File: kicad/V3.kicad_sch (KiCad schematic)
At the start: 5 parts

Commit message: switch
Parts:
- added SW1: Slide_Switch_SPDT_P3mm_10x5x10mm, PCM_SL_Devices:Slide_Switch_SPDT_P3mm_10x5x10mm, symbol PCM_SL_Devices:Slide_Switch_SPDT_P3mm_10x5x10mm
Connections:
- net -3V3: now also SW1.1; no longer U1.1 (Out+)
- new net: SW1.2, U1.1 (Out+)
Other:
- moved on the sheet: BT1
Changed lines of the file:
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@@
 	)
 	(junction
-		(at 218.44 64.77)
+		(at 259.08 39.37)
 		(diameter 0)
 		(color 0 0 0 0)
@@
 	(wire
 		(pts
-			(xy 231.14 53.34) (xy 234.95 53.34)
+			(xy 271.78 27.94) (xy 275.59 27.94)
 		)
 		(stroke
@@
 	(wire
 		(pts
+			(xy 247.65 29.21) (xy 248.92 29.21)
+		)
+		(stroke
+			(width 0)
+			(type default)
+		)
+	)
+	(wire
+		(pts
 			(xy 80.01 50.8) (xy 80.01 72.39)
 		)
@@
 	(wire
 		(pts
-			(xy 218.44 66.04) (xy 218.44 64.77)
+			(xy 259.08 40.64) (xy 259.08 39.37)
 		)
 		(stroke
@@
 	(wire
 		(pts
-			(xy 231.14 53.34) (xy 231.14 54.61)
+			(xy 271.78 27.94) (xy 271.78 29.21)
 		)
 		(stroke
@@
 	(wire
 		(pts
-			(xy 208.28 64.77) (xy 218.44 64.77)
+			(xy 248.92 39.37) (xy 259.08 39.37)
 		)
 		(stroke
@@
 	(wire
 		(pts
-			(xy 208.28 59.69) (xy 208.28 64.77)
+			(xy 248.92 34.29) (xy 248.92 39.37)
 		)
 		(stroke
@@
 	(wire
 		(pts
-			(xy 231.14 60.96) (xy 231.14 59.69)
+			(xy 271.78 35.56) (xy 271.78 34.29)
 		)
 		(stroke
@@
 	(wire
 		(pts
-			(xy 228.6 54.61) (xy 231.14 54.61)
+			(xy 269.24 29.21) (xy 271.78 29.21)
 		)
 		(stroke
@@
 	(wire
 		(pts
-			(xy 231.14 60.96) (xy 234.95 60.96)
+			(xy 271.78 35.56) (xy 275.59 35.56)
 		)
 		(stroke
@@
 	(wire
 		(pts
-			(xy 228.6 59.69) (xy 231.14 59.69)
+			(xy 269.24 34.29) (xy 271.78 34.29)
+		)
+		(stroke
+			(width 0)
+			(type default)
+		)
+	)
+	(wire
+		(pts
+			(xy 236.22 31.75) (xy 236.22 24.13)
 		)
 		(stroke
@@
 	(symbol
 		(lib_id "Library:TP4056_usb_module")
-		(at 215.9 55.88 0)
+		(at 256.54 30.48 0)
 		(unit 1)
 		(exclude_from_sim no)
@@
 		(fields_autoplaced yes)
 		(property "Reference" "U1"
-			(at 214.63 57.15 90)
+			(at 255.27 31.75 90)
 			(effects
 				(font
@@
 		)
 		(property "Value" "~"
-			(at 220.5833 50.8 0)
+			(at 261.2233 25.4 0)
 			(effects
 				(font
@@
 		)
 		(property "Footprint" "Library:HAYATEC TP4056 LIPO CHARGING MODULE"
-			(at 215.9 55.88 0)
+			(at 256.54 30.48 0)
 			(effects
 				(font
@@
 		)
 		(property "Datasheet" ""
-			(at 215.9 55.88 0)
+			(at 256.54 30.48 0)
 			(effects
 				(font
@@
 		)
 		(property "Description" ""
-			(at 215.9 55.88 0)
+			(at 256.54 30.48 0)
 			(effects
 				(font
@@
 	(symbol
 		(lib_id "power:Earth")
-		(at 218.44 66.04 0)
+		(at 259.08 40.64 0)
 		(unit 1)
 		(exclude_from_sim no)
@@
 		(fields_autoplaced yes)
 		(property "Reference" "#PWR01"
-			(at 218.44 72.39 0)
+			(at 259.08 46.99 0)
 			(effects
 				(font
@@
 		)
 		(property "Value" "Earth"
-			(at 218.44 71.12 0)
+			(at 259.08 45.72 0)
 			(effects
 				(font
@@
 		)
 		(property "Footprint" ""
-			(at 218.44 66.04 0)
+			(at 259.08 40.64 0)
 			(effects
 				(font
@@
 		)
 		(property "Datasheet" "~"
-			(at 218.44 66.04 0)
+			(at 259.08 40.64 0)
 			(effects
 				(font
@@
 		)
 		(property "Description" "Power symbol creates a global label with name \"Earth\""
-			(at 218.44 66.04 0)
+			(at 259.08 40.64 0)
 			(effects
 				(font
@@
 	)
 	(symbol
+		(lib_id "PCM_SL_Devices:Slide_Switch_SPDT_P3mm_10x5x10mm")
+		(at 242.57 31.75 0)
+		(unit 1)
+		(exclude_from_sim no)
+		(in_bom yes)
+		(on_board yes)
+		(dnp no)
+		(fields_autoplaced yes)
+		(property "Reference" "SW1"
+			(at 241.935 24.13 0)
+			(effects
+				(font
+					(size 1.27 1.27)
+				)
+			)
+		)
+		(property "Value" "Slide_Switch_SPDT_P3mm_10x5x10mm"
+			(at 241.935 26.67 0)
+			(effects
+				(font
+					(size 1.27 1.27)
+				)
+			)
+		)
+		(property "Footprint" "PCM_SL_Devices:Slide_Switch_SPDT_P3mm_10x5x10mm"
+			(at 243.84 39.37 0)
+			(effects
+				(font
+					(size 1.27 1.27)
+				)
+				(hide yes)
+			)
+		)
+		(property "Datasheet" ""
+			(at 241.3 25.4 0)
+			(effects
+				(font
+					(size 1.27 1.27)
+				)
+				(hide yes)
+			)
+		)
+		(property "Description" "SPDT Slide Switch with 10mm length, 5mm width and 10mm hight."
+			(at 242.57 31.75 0)
+			(effects
+				(font
+					(size 1.27 1.27)
+				)
+				(hide yes)
+			)
+		)
+		(pin "2"
+		)
+		(pin "3"
+		)
+		(pin "1"
+		)
+		(instances
+			(project ""
+				(path "/55ac274f-6d39-4edb-ae03-cf051723ec39"
+					(reference "SW1")
+					(unit 1)
+				)
+			)
+		)
+	)
+	(symbol
 		(lib_id "power:VCC")
-		(at 218.44 49.53 0)
+		(at 259.08 24.13 0)
 		(unit 1)
 		(exclude_from_sim no)
@@
 		(fields_autoplaced yes)
 		(property "Reference" "#PWR03"
-			(at 218.44 53.34 0)
+			(at 259.08 27.94 0)
 			(effects
 				(font
@@
 		)
 		(property "Value" "VCC"
-			(at 218.44 44.45 0)
+			(at 259.08 19.05 0)
 			(effects
 				(font
@@
 		)
 		(property "Footprint" ""
-			(at 218.44 49.53 0)
+			(at 259.08 24.13 0)
 			(effects
 				(font
@@
 		)
 		(property "Datasheet" ""
-			(at 218.44 49.53 0)
+			(at 259.08 24.13 0)
 			(effects
 				(font
@@
 		)
 		(property "Description" "Power symbol creates a global label with name \"VCC\""
-			(at 218.44 49.53 0)
+			(at 259.08 24.13 0)
 			(effects
 				(font
@@
 	(symbol
 		(lib_id "Device:Battery_Cell")
-		(at 234.95 58.42 0)
+		(at 275.59 33.02 0)
 		(unit 1)
 		(exclude_from_sim no)
@@
 		(fields_autoplaced yes)
 		(property "Reference" "BT1"
-			(at 238.76 55.3084 0)
+			(at 279.4 29.9084 0)
 			(effects
 				(font
@@
 		)
 		(property "Value" "Battery_Cell"
-			(at 238.76 57.8484 0)
+			(at 279.4 32.4484 0)
 			(effects
 				(font
@@
 		)
 		(property "Footprint" ""
-			(at 234.95 56.896 90)
+			(at 275.59 31.496 90)
 			(effects
 				(font
@@
 		)
 		(property "Datasheet" "~"
-			(at 234.95 56.896 90)
+			(at 275.59 31.496 90)
 			(effects
 				(font
@@
 		)
 		(property "Description" "Single-cell battery"
-			(at 234.95 58.42 0)
+			(at 275.59 33.02 0)
 			(effects
 				(font
@@
 	(symbol
 		(lib_id "power:-3V3")
-		(at 208.28 54.61 0)
+		(at 236.22 24.13 0)
 		(unit 1)
 		(exclude_from_sim no)
@@
 		(fields_autoplaced yes)
 		(property "Reference" "#PWR08"
-			(at 208.28 58.42 0)
+			(at 236.22 27.94 0)
 			(effects
 				(font
@@
 		)
 		(property "Value" "-3V3"
-			(at 208.28 49.53 0)
+			(at 236.22 19.05 0)
 			(effects
 				(font
@@
 		)
 		(property "Footprint" ""
-			(at 208.28 54.61 0)
+			(at 236.22 24.13 0)
 			(effects
 				(font
@@
 		)
 		(property "Datasheet" ""
-			(at 208.28 54.61 0)
+			(at 236.22 24.13 0)
 			(effects
 				(font
@@
 		)
 		(property "Description" "Power symbol creates a global label with name \"-3V3\""
-			(at 208.28 54.61 0)
-			(effects
-				(font
+			(at 236.22 24.13 0)
+			(effects
+				(font

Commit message: fixed connections and pin#
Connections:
- net Earth: now also U1.1 (Gin), U1.3 (Out-); no longer U1.2 (Gin), U1.5 (Out-)
- net VCC: now also U1.2 (Vin); no longer U1.4 (Vin)
- net at SW1.2: now also U1.6 (Out+); no longer U1.1 (Out+)
- net at BT1.1 (+): now also U1.5 (B+); no longer U1.3 (B+)
- net at BT1.2 (-): now also U1.4 (B-); no longer U1.6 (B-)
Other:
- moved on the sheet: SW1
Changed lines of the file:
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@@
+	)
+	(junction
+		(at 259.08 39.37)
+		(diameter 0)
+		(color 0 0 0 0)
 	)
 	(junction
@@
 	)
 	(junction
-		(at 259.08 39.37)
-		(diameter 0)
-		(color 0 0 0 0)
-	)
-	(junction
 		(at 118.11 90.17)
 		(diameter 0)
@@
 	(wire
 		(pts
-			(xy 247.65 29.21) (xy 248.92 29.21)
+			(xy 242.57 29.21) (xy 248.92 29.21)
 		)
 		(stroke
@@
 	(wire
 		(pts
-			(xy 236.22 31.75) (xy 236.22 24.13)
+			(xy 231.14 31.75) (xy 231.14 24.13)
 		)
 		(stroke
@@
 			)
 		)
+		(pin "3"
+		)
+		(pin "5"
+		)
+		(pin "2"
+		)
+		(pin "6"
+		)
 		(pin "1"
 		)
-		(pin "6"
-		)
-		(pin "3"
-		)
 		(pin "4"
-		)
-		(pin "2"
-		)
-		(pin "5"
 		)
 		(instances
@@
 	(symbol
 		(lib_id "PCM_SL_Devices:Slide_Switch_SPDT_P3mm_10x5x10mm")
-		(at 242.57 31.75 0)
+		(at 237.49 31.75 0)
 		(unit 1)
 		(exclude_from_sim no)
@@
 		(fields_autoplaced yes)
 		(property "Reference" "SW1"
-			(at 241.935 24.13 0)
+			(at 236.855 24.13 0)
 			(effects
 				(font
@@
 		)
 		(property "Value" "Slide_Switch_SPDT_P3mm_10x5x10mm"
-			(at 241.935 26.67 0)
+			(at 236.855 26.67 0)
 			(effects
 				(font
@@
 		)
 		(property "Footprint" "PCM_SL_Devices:Slide_Switch_SPDT_P3mm_10x5x10mm"
-			(at 243.84 39.37 0)
+			(at 238.76 39.37 0)
 			(effects
 				(font
@@
 		)
 		(property "Datasheet" ""
-			(at 241.3 25.4 0)
+			(at 236.22 25.4 0)
 			(effects
 				(font
@@
 		)
 		(property "Description" "SPDT Slide Switch with 10mm length, 5mm width and 10mm hight."
-			(at 242.57 31.75 0)
+			(at 237.49 31.75 0)
 			(effects
 				(font
@@
 	(symbol
 		(lib_id "power:-3V3")
-		(at 236.22 24.13 0)
+		(at 231.14 24.13 0)
 		(unit 1)
 		(exclude_from_sim no)
@@
 		(fields_autoplaced yes)
 		(property "Reference" "#PWR08"
-			(at 236.22 27.94 0)
+			(at 231.14 27.94 0)
 			(effects
 				(font
@@
 		)
 		(property "Value" "-3V3"
-			(at 236.22 19.05 0)
+			(at 231.14 19.05 0)
 			(effects
 				(font
@@
 		)
 		(property "Footprint" ""
-			(at 236.22 24.13 0)
+			(at 231.14 24.13 0)
 			(effects
 				(font
@@
 		)
 		(property "Datasheet" ""
-			(at 236.22 24.13 0)
+			(at 231.14 24.13 0)
 			(effects
 				(font
@@
 		)
 		(property "Description" "Power symbol creates a global label with name \"-3V3\""
-			(at 236.22 24.13 0)
-			(effects
-				(font
+			(at 231.14 24.13 0)
+			(effects
+				(font

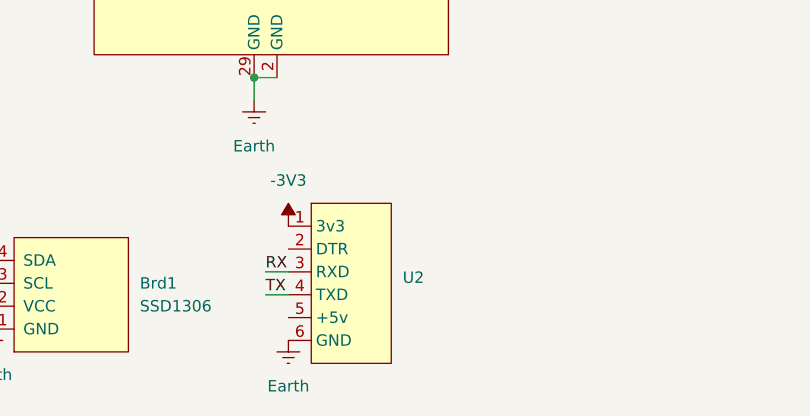
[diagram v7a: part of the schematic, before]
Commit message: changed uart-hid pinout
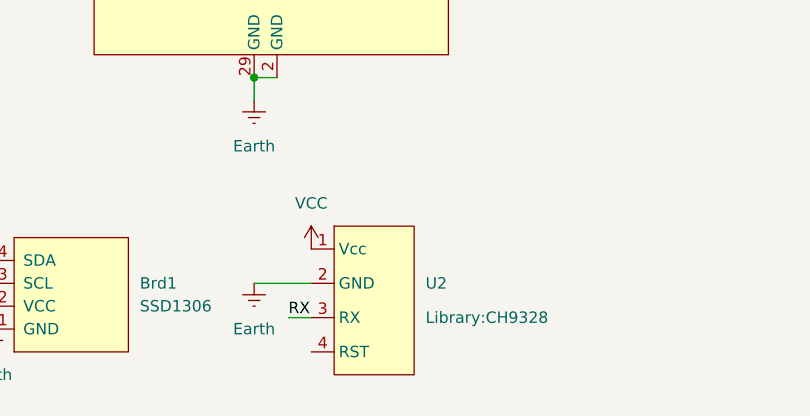
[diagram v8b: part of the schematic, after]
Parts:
- removed U2: ~, Library:CH340C_pins, symbol Library:CH340C_usb_module
- added U2: ~, Library:CH9328, symbol Library:CH9328
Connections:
- net Earth: now also U2.2 (GND)
- net RX: now also U2.3 (RX)
- net VCC: now also U2.1 (Vcc)
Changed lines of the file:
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@@
 	(wire
 		(pts
-			(xy 165.1 121.92) (xy 167.64 121.92)
+			(xy 167.64 127) (xy 170.18 127)
 		)
 		(stroke
@@
 	(wire
 		(pts
+			(xy 163.83 123.19) (xy 170.18 123.19)
+		)
+		(stroke
+			(width 0)
+			(type default)
+		)
+	)
+	(wire
+		(pts
 			(xy 125.73 125.73) (xy 134.62 125.73)
 		)
@@
 	(wire
 		(pts
-			(xy 165.1 124.46) (xy 167.64 124.46)
-		)
-		(stroke
-			(width 0)
-			(type default)
-		)
-	)
-	(wire
-		(pts
 			(xy 95.25 127) (xy 95.25 129.54)
 		)
@@
 	)
 	(label "RX"
-		(at 165.1 121.92 0)
+		(at 167.64 127 0)
 		(effects
 			(font
@@
 	(label "SDA"
 		(at 138.43 71.12 0)
-		(effects
-			(font
-				(size 1.27 1.27)
-			)
-			(justify left bottom)
-		)
-	)
-	(label "TX"
-		(at 165.1 124.46 0)
 		(effects
 			(font
@@
 	)
 	(symbol
+		(lib_id "power:VCC")
+		(at 170.18 119.38 0)
+		(unit 1)
+		(exclude_from_sim no)
+		(in_bom yes)
+		(on_board yes)
+		(dnp no)
+		(fields_autoplaced yes)
+		(property "Reference" "#PWR09"
+			(at 170.18 123.19 0)
+			(effects
+				(font
+					(size 1.27 1.27)
+				)
+				(hide yes)
+			)
+		)
+		(property "Value" "VCC"
+			(at 170.18 114.3 0)
+			(effects
+				(font
+					(size 1.27 1.27)
+				)
+			)
+		)
+		(property "Footprint" ""
+			(at 170.18 119.38 0)
+			(effects
+				(font
+					(size 1.27 1.27)
+				)
+				(hide yes)
+			)
+		)
+		(property "Datasheet" ""
+			(at 170.18 119.38 0)
+			(effects
+				(font
+					(size 1.27 1.27)
+				)
+				(hide yes)
+			)
+		)
+		(property "Description" "Power symbol creates a global label with name \"VCC\""
+			(at 170.18 119.38 0)
+			(effects
+				(font
+					(size 1.27 1.27)
+				)
+				(hide yes)
+			)
+		)
+		(pin "1"
+		)
+		(instances
+			(project "V3"
+				(path "/55ac274f-6d39-4edb-ae03-cf051723ec39"
+					(reference "#PWR09")
+					(unit 1)
+				)
+			)
+		)
+	)
+	(symbol
 		(lib_id "Librarie:SSD1306")
 		(at 143.51 124.46 90)
@@
 	)
 	(symbol
-		(lib_id "Library:CH340C_usb_module")
-		(at 171.45 121.92 0)
-		(unit 1)
-		(exclude_from_sim no)
-		(in_bom yes)
-		(on_board yes)
-		(dnp no)
-		(fields_autoplaced yes)
-		(property "Reference" "U2"
-			(at 180.34 122.5549 0)
-			(effects
-				(font
-					(size 1.27 1.27)
-				)
-				(justify left)
-			)
-		)
-		(property "Value" "~"
-			(at 180.34 124.46 0)
-			(effects
-				(font
-					(size 1.27 1.27)
-				)
-				(justify left)
-			)
-		)
-		(property "Footprint" "Library:CH340C_pins"
-			(at 171.45 121.92 0)
-			(effects
-				(font
-					(size 1.27 1.27)
-				)
-				(hide yes)
-			)
-		)
-		(property "Datasheet" ""
-			(at 171.45 121.92 0)
-			(effects
-				(font
-					(size 1.27 1.27)
-				)
-				(hide yes)
-			)
-		)
-		(property "Description" ""
-			(at 171.45 121.92 0)
-			(effects
-				(font
-					(size 1.27 1.27)
-				)
-				(hide yes)
-			)
-		)
-		(pin "4"
-		)
-		(pin "1"
-		)
-		(pin "2"
-		)
-		(pin "3"
-		)
-		(pin "5"
-		)
-		(pin "6"
-		)
-		(instances
-			(project ""
-				(path "/55ac274f-6d39-4edb-ae03-cf051723ec39"
-					(reference "U2")
-					(unit 1)
-				)
-			)
-		)
-	)
-	(symbol
 		(lib_id "power:Earth")
 		(at 259.08 40.64 0)
@@
 	)
 	(symbol
+		(lib_id "Library:CH9328")
+		(at 180.34 125.73 0)
+		(unit 1)
+		(exclude_from_sim no)
+		(in_bom yes)
+		(on_board yes)
+		(dnp no)
+		(fields_autoplaced yes)
+		(property "Reference" "U2"
+			(at 182.88 123.1899 0)
+			(effects
+				(font
+					(size 1.27 1.27)
+				)
+				(justify left)
+			)
+		)
+		(property "Value" "~"
+			(at 182.88 125.095 0)
+			(effects
+				(font
+					(size 1.27 1.27)
+				)
+				(justify left)
+			)
+		)
+		(property "Footprint" "Library:CH9328"
+			(at 182.88 126.9999 0)
+			(effects
+				(font
+					(size 1.27 1.27)
+				)
+				(justify left)
+			)
+		)
+		(property "Datasheet" ""
+			(at 180.34 125.73 0)
+			(effects
+				(font
+					(size 1.27 1.27)
+				)
+				(hide yes)
+			)
+		)
+		(property "Description" ""
+			(at 180.34 125.73 0)
+			(effects
+				(font
+					(size 1.27 1.27)
+				)
+				(hide yes)
+			)
+		)
+		(pin "2"
+		)
+		(pin "3"
+		)
+		(pin "4"
+		)
+		(pin "1"
+		)
+		(instances
+			(project ""
+				(path "/55ac274f-6d39-4edb-ae03-cf051723ec39"
+					(reference "U2")
+					(unit 1)
+				)
+			)
+		)
+	)
+	(symbol
 		(lib_id "PCM_SL_Devices:Slide_Switch_SPDT_P3mm_10x5x10mm")
 		(at 237.49 31.75 0)
@@
 	)
 	(symbol
-		(lib_id "power:-3V3")
-		(at 167.64 116.84 0)
-		(unit 1)
-		(exclude_from_sim no)
-		(in_bom yes)
-		(on_board yes)
-		(dnp no)
-		(fields_autoplaced yes)
-		(property "Reference" "#PWR09"
-			(at 167.64 120.65 0)
-			(effects
-				(font
-					(size 1.27 1.27)
-				)
-				(hide yes)
-			)
-		)
-		(property "Value" "-3V3"
-			(at 167.64 111.76 0)
-			(effects
-				(font
-					(size 1.27 1.27)
-				)
-			)
-		)
-		(property "Footprint" ""
-			(at 167.64 116.84 0)
-			(effects
-				(font
-					(size 1.27 1.27)
-				)
-				(hide yes)
-			)
-		)
-		(property "Datasheet" ""
-			(at 167.64 116.84 0)
-			(effects
-				(font
-					(size 1.27 1.27)
-				)
-				(hide yes)
-			)
-		)
-		(property "Description" "Power symbol creates a global label with name \"-3V3\""
-			(at 167.64 116.84 0)
-			(effects
-				(font
-					(size 1.27 1.27)
-				)
-				(hide yes)
-			)
-		)
-		(pin "1"
-		)
-		(instances
-			(project "V3"
-				(path "/55ac274f-6d39-4edb-ae03-cf051723ec39"
-					(reference "#PWR09")
-					(unit 1)
-				)
-			)
-		)
-	)
-	(symbol
 		(lib_id "power:Earth")
-		(at 167.64 129.54 0)
+		(at 163.83 123.19 0)
 		(unit 1)
 		(exclude_from_sim no)
@@
 		(fields_autoplaced yes)
 		(property "Reference" "#PWR010"
-			(at 167.64 135.89 0)
+			(at 163.83 129.54 0)
 			(effects
 				(font
@@
 		)
 		(property "Value" "Earth"
-			(at 167.64 134.62 0)
+			(at 163.83 128.27 0)
 			(effects
 				(font
@@
 		)
 		(property "Footprint" ""
-			(at 167.64 129.54 0)
+			(at 163.83 123.19 0)
 			(effects
 				(font
@@
 		)
 		(property "Datasheet" "~"
-			(at 167.64 129.54 0)
+			(at 163.83 123.19 0)
 			(effects
 				(font
@@
 		)
 		(property "Description" "Power symbol creates a global label with name \"Earth\""
-			(at 167.64 129.54 0)
-			(effects
-				(font
+			(at 163.83 123.19 0)
+			(effects
+				(font
